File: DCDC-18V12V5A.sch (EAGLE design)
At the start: 38 parts, among them Q10 NMOSFET, Q9 NMOSFET, U1 LM3150MHX/NOPB

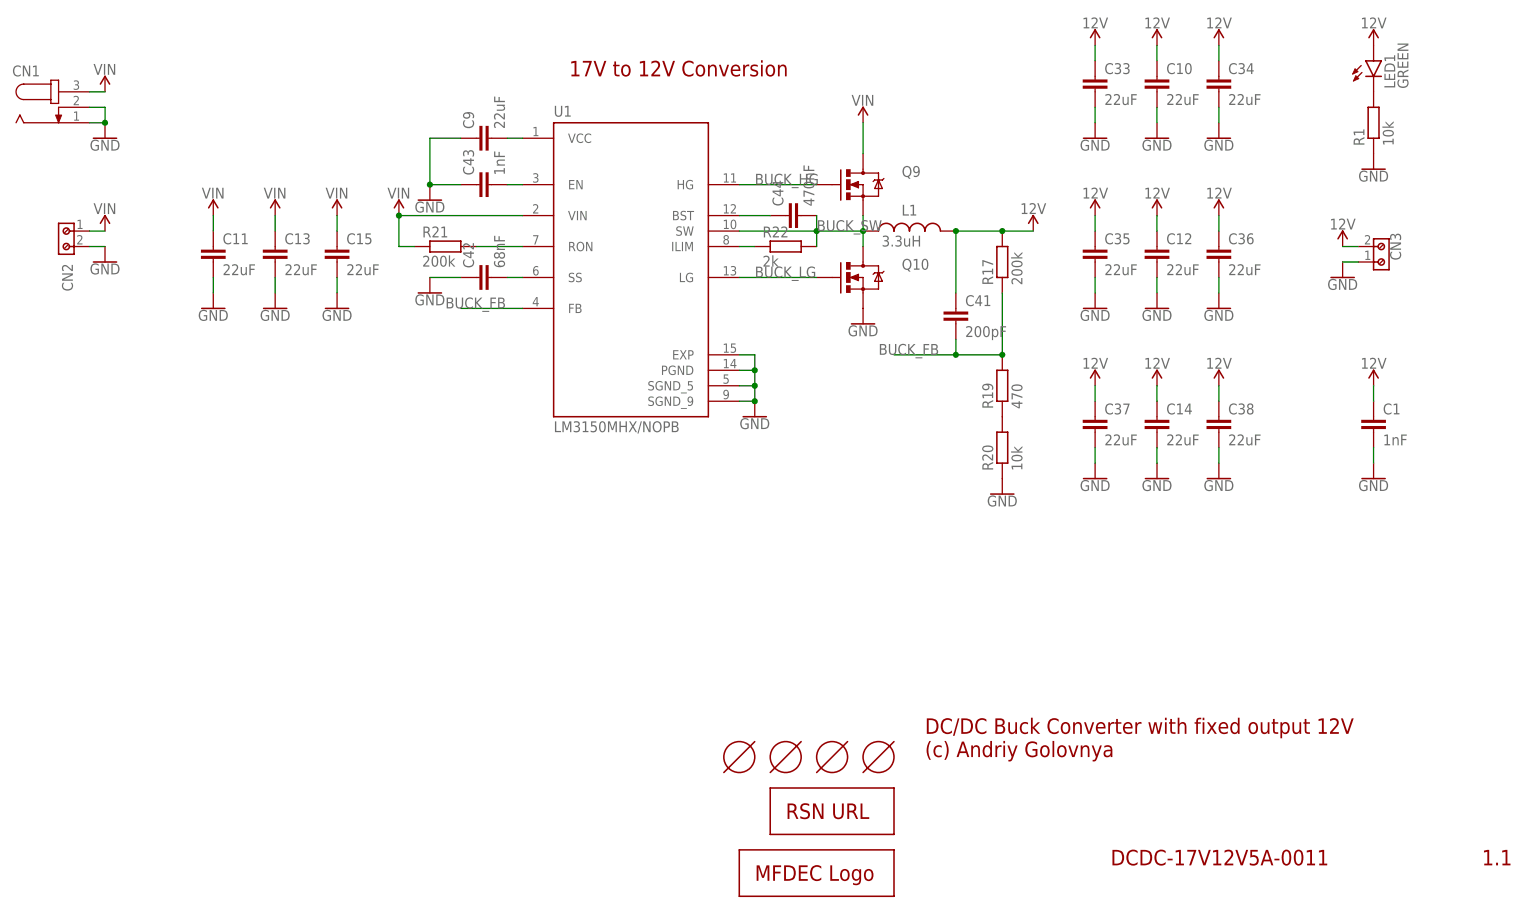
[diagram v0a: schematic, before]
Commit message: Changed texts on 18V-12V boards. Generated CAM files. Generated PNG preview. Generated PDF schematics.
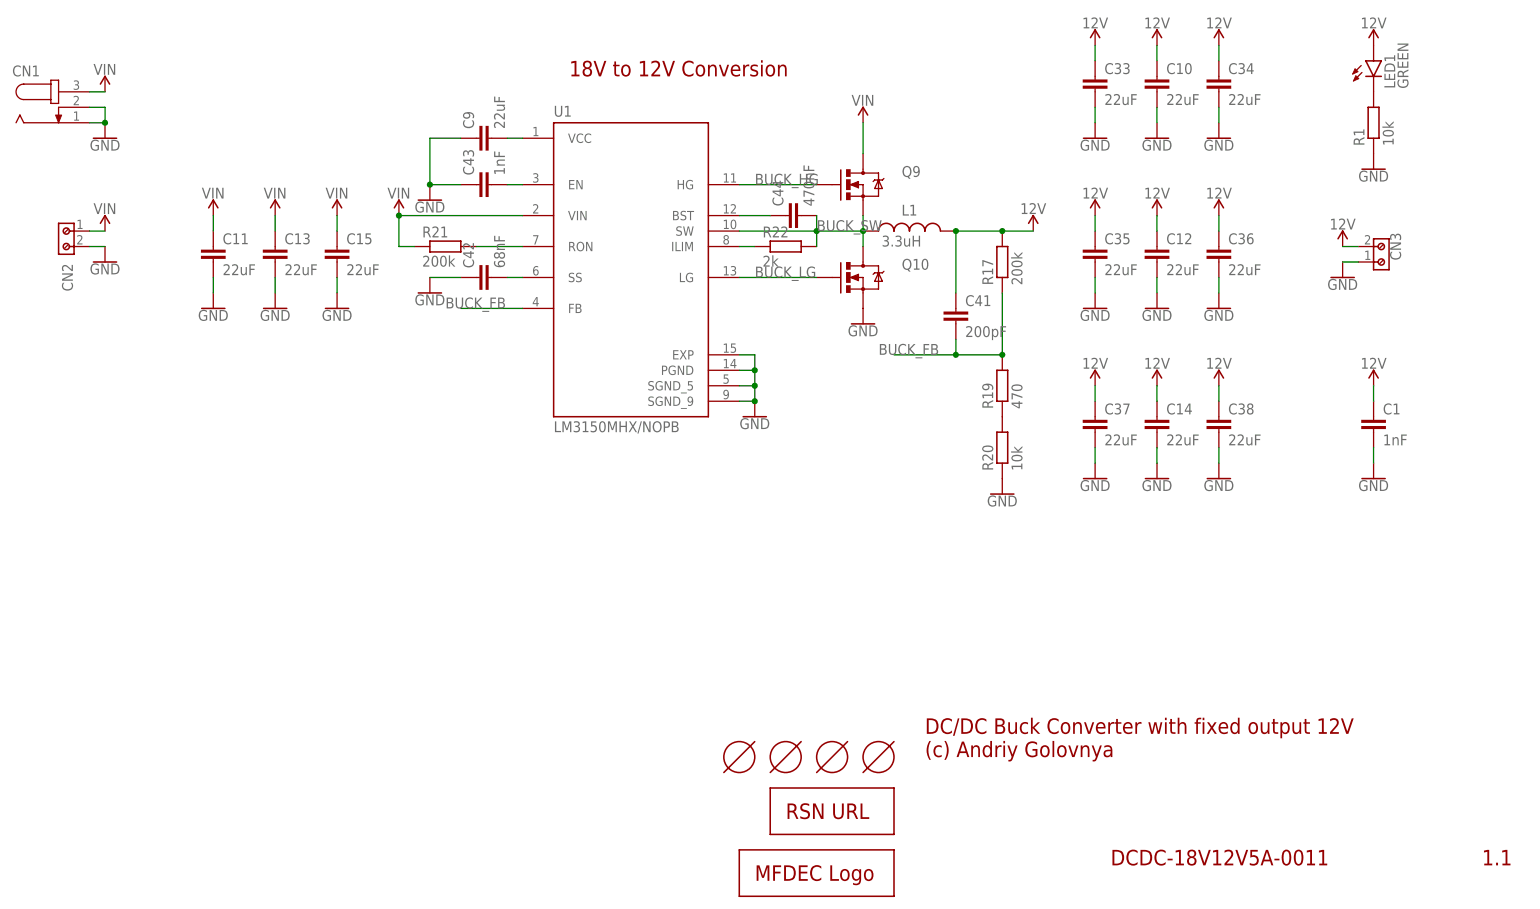
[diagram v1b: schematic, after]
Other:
- note added: "18V to 12V Conversion"
- note added: "DCDC-18V12V5A-0011"
- note removed: "17V to 12V Conversion"
- note removed: "DCDC-17V12V5A-0011"
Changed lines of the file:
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@@
 <plain>
 <text x="256.54" y="7.62" size="2.54" layer="94">1.1</text>
-<text x="195.58" y="7.62" size="2.54" layer="94">DCDC-17V12V5A-0011</text>
+<text x="195.58" y="7.62" size="2.54" layer="94">DCDC-18V12V5A-0011</text>
 <text x="165.1" y="25.4" size="2.54" layer="94">DC/DC Buck Converter with fixed output 12V
 (c) Andriy Golovnya</text>
-<text x="106.68" y="137.16" size="2.54" layer="94">17V to 12V Conversion</text>
+<text x="106.68" y="137.16" size="2.54" layer="94">18V to 12V Conversion</text>
 </plain>
 <instances>
